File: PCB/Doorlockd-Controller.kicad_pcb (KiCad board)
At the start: 2 copper layers, 132 x 103 mm, 60 parts, among them J1 MilkV P43 (3.3V for VCCB), J10 Power Out 1, J11 DC in, J12 IO 3, J13 Debug UART, J14 IO 4, J15 Power Out 2, J16 to extra screw conn., J18 GPIO only MilkV 1.8V, J19 3V 5V Vin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

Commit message: Cosmetic PCB changes
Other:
- outline, holes or cut-outs redrawn
- board text added: "5V RX TX"

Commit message: Replace STU60N3LH5 FET with STD12NF06L-1
The former is not available anymore since a while, the latter is
another IPAK FET with similar specs.
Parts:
- Q2, Q5: value STU60N3LH5 -> STD12NF06L-1
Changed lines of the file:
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@@
 			)
 		)
-		(property "Value" "STU60N3LH5"
+		(property "Value" "STD12NF06L-1"
 			(at 2.286 2.15 0)
 			(layer "F.Fab")
@@
 			)
 		)
-		(property "Value" "STU60N3LH5"
+		(property "Value" "STD12NF06L-1"
 			(at 2.286 2.15 0)
 			(layer "F.Fab")

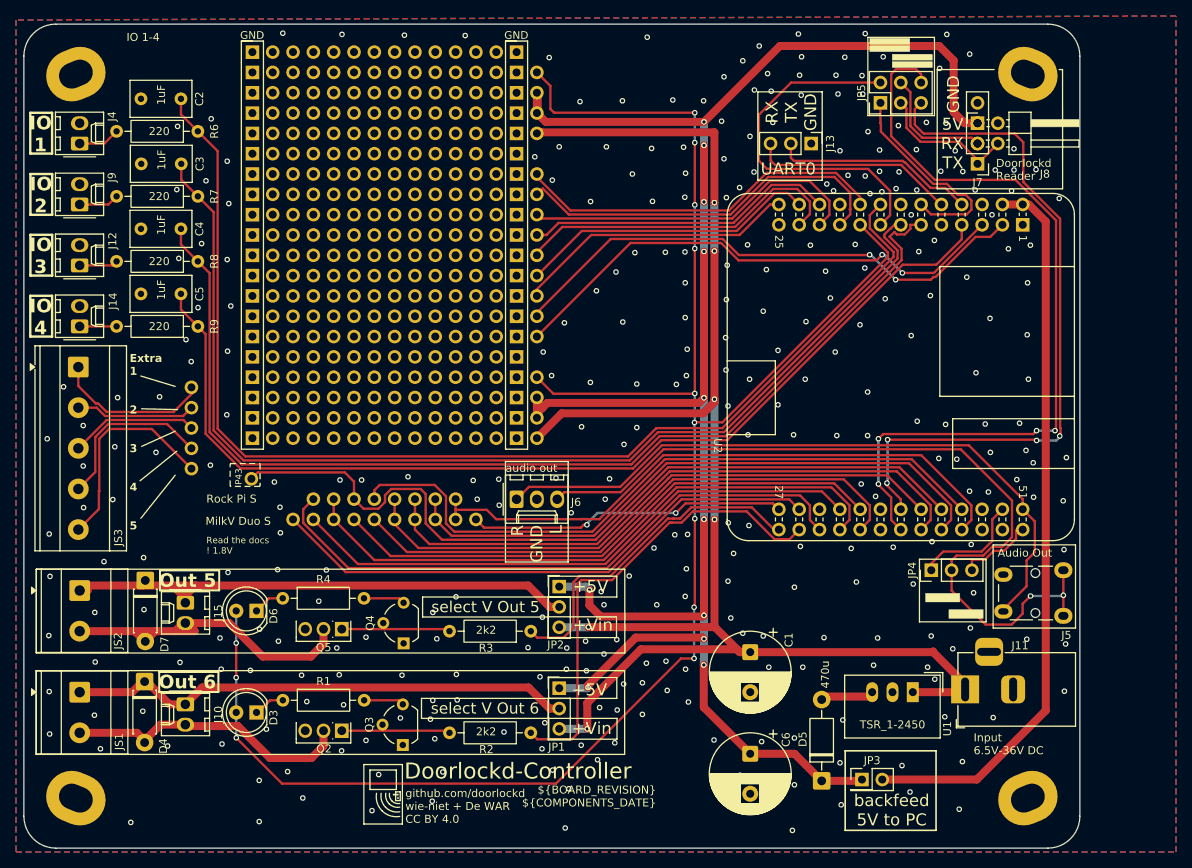
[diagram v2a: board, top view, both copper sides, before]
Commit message: Improve mounting hole accuracy
Turns out these holes were actually 26.565 degrees (atan(0.5)), not 22.5.
This fixes the footprint to angle the pad at 26.5 and puts the courtyard
and user comments figures in the exactly correct spot.

This also renames the footprint, switching from specifying the angle
(which would be inexact) to the center offset of the second hole.
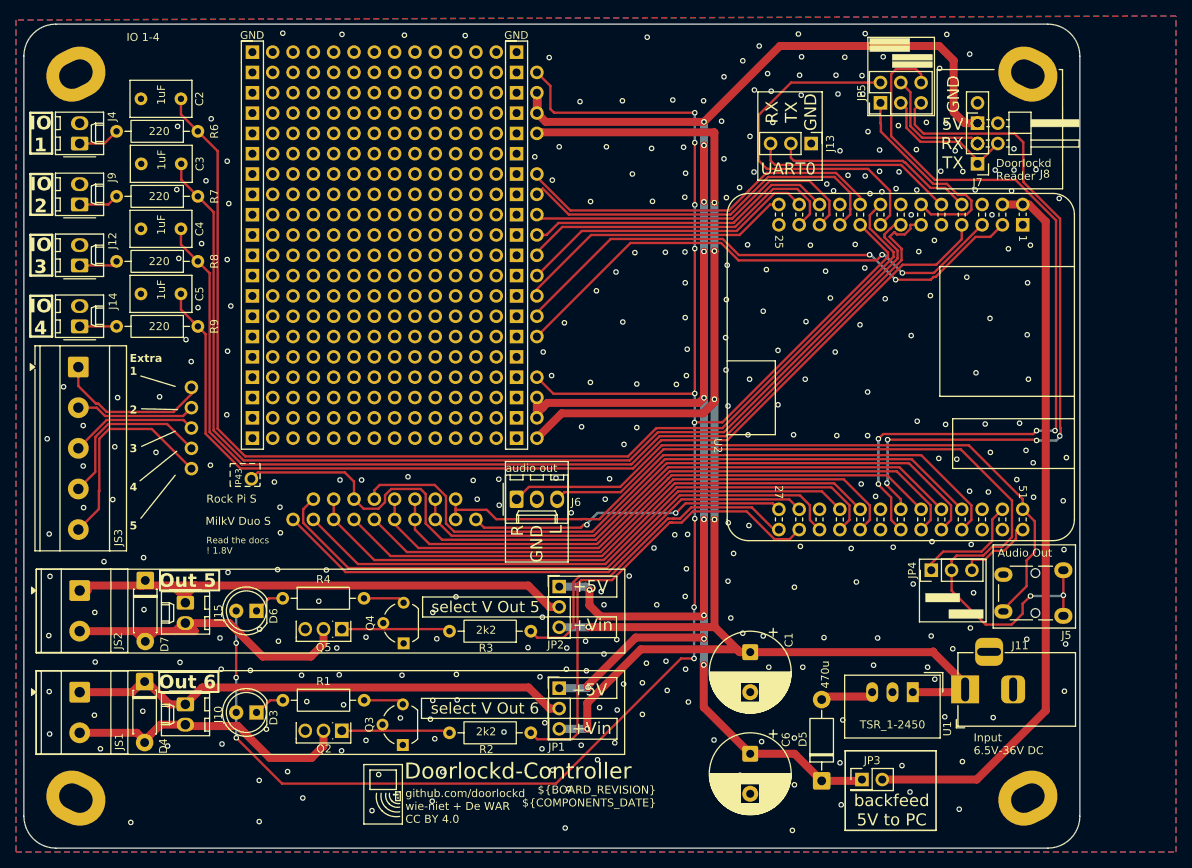
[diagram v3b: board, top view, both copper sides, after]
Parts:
- H1, H2, H3, H4: footprint MountingHole_3.2x4.32mm_Oval_22.5deg:MountingHole_3.2x4.32mm_Oval_22.5deg -> MountingHole_Dual_3.2mm_M3_Offset1x0.5mm:MountingHole_Dual_3.2mm_M3_Offset1x0.5mm
